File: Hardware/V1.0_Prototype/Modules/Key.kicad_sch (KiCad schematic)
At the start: 3 parts, among them SW1 SW_HotSwap

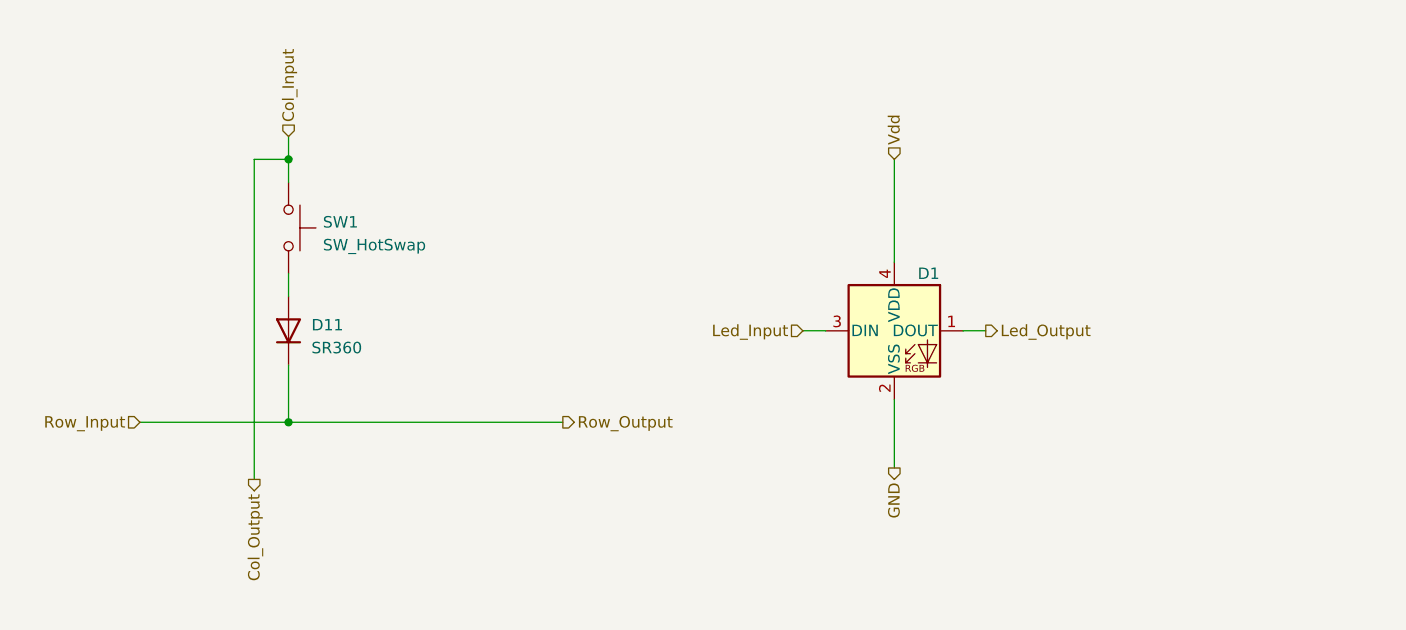
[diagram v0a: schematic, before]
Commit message: update repo, add proto PCB
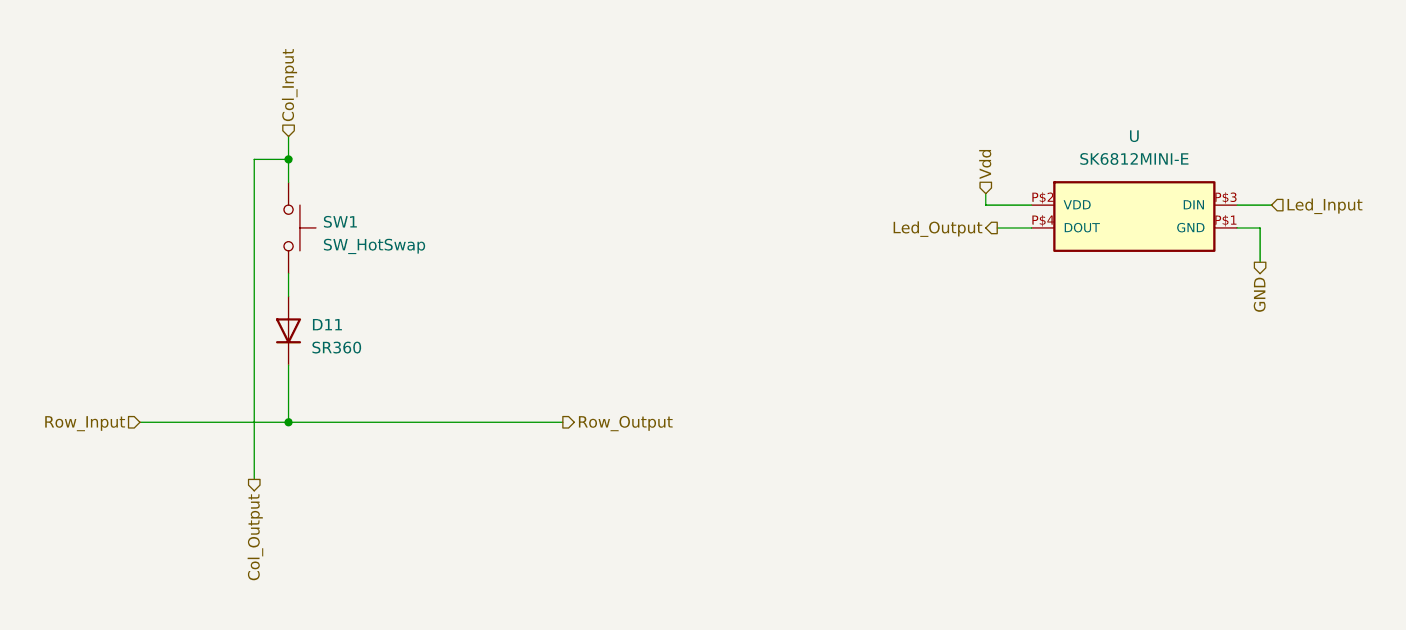
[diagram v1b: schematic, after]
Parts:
- removed D1: SK6812MINI-E, LED_SMD:LED_SK6812MINI_PLCC4_3.5x3.5mm_P1.75mm, symbol LED:SK6812MINI
- added U: SK6812MINI-E, CREPP_LEDs:SK6812MINI-E, symbol CREPP_LED:SK6812MINI-E
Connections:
- net GND: now also U.P$1 (GND)
- net Led_Input: now also U.P$3 (DIN)
- net Led_Output: now also U.P$4 (DOUT)
- net Vdd: now also U.P$2 (VDD)
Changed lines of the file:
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@@
 (kicad_sch
-	(version 20231120)
+	(version 20250114)
 	(generator "eeschema")
-	(generator_version "8.0")
+	(generator_version "9.0")
 	(paper "A5")
 	(title_block
@@
 	(wire
 		(pts
-			(xy 118.11 62.23) (xy 120.65 62.23)
-		)
-		(stroke
-			(width 0)
-			(type default)
-		)
-	)
-	(wire
-		(pts
-			(xy 128.27 69.85) (xy 128.27 77.47)
+			(xy 139.7 50.8) (xy 143.51 50.8)
 		)
 		(stroke
@@
 	(wire
 		(pts
-			(xy 135.89 62.23) (xy 138.43 62.23)
-		)
-		(stroke
-			(width 0)
-			(type default)
-		)
-	)
-	(wire
-		(pts
 			(xy 44.45 72.39) (xy 60.96 72.39)
 		)
@@
 	(wire
 		(pts
-			(xy 128.27 43.18) (xy 128.27 54.61)
+			(xy 166.37 48.26) (xy 170.18 48.26)
 		)
 		(stroke
@@
 	(wire
 		(pts
+			(xy 138.43 48.26) (xy 138.43 46.99)
+		)
+		(stroke
+			(width 0)
+			(type default)
+		)
+	)
+	(wire
+		(pts
 			(xy 60.96 40.64) (xy 60.96 43.18)
 		)
@@
 		(pts
 			(xy 57.15 43.18) (xy 60.96 43.18)
+		)
+		(stroke
+			(width 0)
+			(type default)
+		)
+	)
+	(wire
+		(pts
+			(xy 166.37 50.8) (xy 168.91 50.8)
+		)
+		(stroke
+			(width 0)
+			(type default)
+		)
+	)
+	(wire
+		(pts
+			(xy 143.51 48.26) (xy 138.43 48.26)
+		)
+		(stroke
+			(width 0)
+			(type default)
+		)
+	)
+	(wire
+		(pts
+			(xy 168.91 50.8) (xy 168.91 54.61)
 		)
 		(stroke
@@
 	(hierarchical_label "Led_Input"
 		(shape input)
-		(at 118.11 62.23 180)
-		(fields_autoplaced yes)
-		(effects
-			(font
-				(size 1.27 1.27)
-			)
-			(justify right)
+		(at 170.18 48.26 0)
+		(effects
+			(font
+				(size 1.27 1.27)
+			)
+			(justify left)
 		)
 	)
 	(hierarchical_label "Vdd"
 		(shape input)
-		(at 128.27 43.18 90)
-		(fields_autoplaced yes)
+		(at 138.43 46.99 90)
 		(effects
 			(font
@@
 		(shape output)
 		(at 91.44 72.39 0)
-		(fields_autoplaced yes)
 		(effects
 			(font
@@
 		(shape input)
 		(at 60.96 40.64 90)
-		(fields_autoplaced yes)
 		(effects
 			(font
@@
 		(shape input)
 		(at 44.45 72.39 180)
-		(fields_autoplaced yes)
 		(effects
 			(font
@@
 	(hierarchical_label "GND"
 		(shape output)
-		(at 128.27 77.47 270)
-		(fields_autoplaced yes)
+		(at 168.91 54.61 270)
 		(effects
 			(font
@@
 		(shape output)
 		(at 57.15 78.74 270)
-		(fields_autoplaced yes)
 		(effects
 			(font
@@
 	(hierarchical_label "Led_Output"
 		(shape output)
-		(at 138.43 62.23 0)
-		(fields_autoplaced yes)
-		(effects
-			(font
-				(size 1.27 1.27)
-			)
-			(justify left)
+		(at 139.7 50.8 180)
+		(effects
+			(font
+				(size 1.27 1.27)
+			)
+			(justify right)
 		)
 	)
@@
 					(unit 1)
 				)
+				(path "/fd8c8265-4947-4b90-b980-57cac1b7867b/9991b651-e787-4efe-9cad-372e4ec6057a"
+					(reference "D7")
+					(unit 1)
+				)
+				(path "/fd8c8265-4947-4b90-b980-57cac1b7867b/bf661854-ca2a-4e94-82fd-5ee2763dff01"
+					(reference "D6")
+					(unit 1)
+				)
+				(path "/fd8c8265-4947-4b90-b980-57cac1b7867b/d10249f7-e9a3-4816-9659-60ba6a668675"
+					(reference "D8")
+					(unit 1)
+				)
 			)
 		)
@@
 					(unit 1)
 				)
+				(path "/fd8c8265-4947-4b90-b980-57cac1b7867b/9991b651-e787-4efe-9cad-372e4ec6057a"
+					(reference "SW3")
+					(unit 1)
+				)
+				(path "/fd8c8265-4947-4b90-b980-57cac1b7867b/bf661854-ca2a-4e94-82fd-5ee2763dff01"
+					(reference "SW2")
+					(unit 1)
+				)
+				(path "/fd8c8265-4947-4b90-b980-57cac1b7867b/d10249f7-e9a3-4816-9659-60ba6a668675"
+					(reference "SW4")
+					(unit 1)
+				)
 			)
 		)
 	)
 	(symbol
-		(lib_id "LED:SK6812MINI")
-		(at 128.27 62.23 0)
+		(lib_id "CREPP_LED:SK6812MINI-E")
+		(at 153.67 48.26 0)
 		(unit 1)
 		(exclude_from_sim no)
@@
 		(on_board yes)
 		(dnp no)
-		(property "Reference" "D1"
-			(at 132.08 55.88 0)
+		(fields_autoplaced yes)
+		(property "Reference" "U"
+			(at 154.94 40.64 0)
 			(effects
 				(font
@@
 		)
 		(property "Value" "SK6812MINI-E"
-			(at 140.97 61.6459 0)
-			(effects
-				(font
-					(size 1.27 1.27)
-				)
-				(hide yes)
-			)
-		)
-		(property "Footprint" "LED_SMD:LED_SK6812MINI_PLCC4_3.5x3.5mm_P1.75mm"
-			(at 129.54 69.85 0)
-			(effects
-				(font
-					(size 1.27 1.27)
-				)
-				(justify left top)
-				(hide yes)
-			)
-		)
-		(property "Datasheet" "https://cdn-shop.adafruit.com/product-files/2686/SK6812MINI_REV.01-1-2.pdf"
-			(at 130.81 71.755 0)
-			(effects
-				(font
-					(size 1.27 1.27)
-				)
-				(justify left top)
+			(at 154.94 43.18 0)
+			(effects
+				(font
+					(size 1.27 1.27)
+				)
+			)
+		)
+		(property "Footprint" "CREPP_LEDs:SK6812MINI-E"
+			(at 153.67 48.26 0)
+			(effects
+				(font
+					(size 1.27 1.27)
+				)
+				(hide yes)
+			)
+		)
+		(property "Datasheet" ""
+			(at 153.67 48.26 0)
+			(effects
+				(font
+					(size 1.27 1.27)
+				)
 				(hide yes)
 			)
 		)
 		(property "Description" ""
-			(at 128.27 62.23 0)
-			(effects
-				(font
-					(size 1.27 1.27)
-				)
-				(hide yes)
-			)
-		)
-		(pin "1"
-		)
-		(pin "2"
-		)
-		(pin "3"
-		)
-		(pin "4"
+			(at 153.67 48.26 0)
+			(effects
+				(font
+					(size 1.27 1.27)
+				)
+				(hide yes)
+			)
+		)
+		(property "MF" "dongguan occidental optoelectronics"
+			(at 153.67 48.26 0)
+			(effects
+				(font
+					(size 1.27 1.27)
+				)
+				(justify bottom)
+				(hide yes)
+			)
+		)
+		(property "Description_1" ""
+			(at 153.67 48.26 0)
+			(effects
+				(font
+					(size 1.27 1.27)
+				)
+				(justify bottom)
+				(hide yes)
+			)
+		)
+		(property "Package" "None"
+			(at 153.67 48.26 0)
+			(effects
+				(font
+					(size 1.27 1.27)
+				)
+				(justify bottom)
+				(hide yes)
+			)
+		)
+		(property "Price" "None"
+			(at 153.67 48.26 0)
+			(effects
+				(font
+					(size 1.27 1.27)
+				)
+				(justify bottom)
+				(hide yes)
+			)
+		)
+		(property "SnapEDA_Link" "https://www.snapeda.com/parts/SK6812MINI-E/Luna+Optoelectronics/view-part/?ref=snap"
+			(at 153.67 48.26 0)
+			(effects
+				(font
+					(size 1.27 1.27)
+				)
+				(justify bottom)
+				(hide yes)
+			)
+		)
+		(property "MP" "SK6812MINI-E"
+			(at 153.67 48.26 0)
+			(effects
+				(font
+					(size 1.27 1.27)
+				)
+				(justify bottom)
+				(hide yes)
+			)
+		)
+		(property "Availability" "Not in stock"
+			(at 153.67 48.26 0)
+			(effects
+				(font
+					(size 1.27 1.27)
+				)
+				(justify bottom)
+				(hide yes)
+			)
+		)
+		(property "Check_prices" "https://www.snapeda.com/parts/SK6812MINI-E/Luna+Optoelectronics/view-part/?ref=eda"
+			(at 153.67 48.26 0)
+			(effects
+				(font
+					(size 1.27 1.27)
+				)
+				(justify bottom)
+				(hide yes)
+			)
+		)
+		(pin "P$3"
+		)
+		(pin "P$4"
+		)
+		(pin "P$1"
+		)
+		(pin "P$2"
 		)
 		(instances
 			(project "PCB"
-				(path "/fd8c8265-4947-4b90-b980-57cac1b7867b/416eee54-53c7-4fdf-9784-49e18a35f298"
-					(reference "D1")
-					(unit 1)
-				)
+				(path "/fd8c8265-4947-4b90-b980-57cac1b7867b/9991b651-e787-4efe-9cad-372e4ec6057a"
+					(reference "U15")
+					(unit 1)
+				)
+				(path "/fd8c8265-4947-4b90-b980-57cac1b7867b/bf661854-ca2a-4e94-82fd-5ee2763dff01"
+					(reference "U12")
+					(unit 1)
+				)
+				(path "/fd8c8265-4947-4b90-b980-57cac1b7867b/d10249f7-e9a3-4816-9659-60ba6a668675"
+					(reference "U16")
+					(unit 1)
+				)
